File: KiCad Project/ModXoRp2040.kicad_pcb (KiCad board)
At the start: 2 copper layers, 38 x 34.8 mm, 0 parts

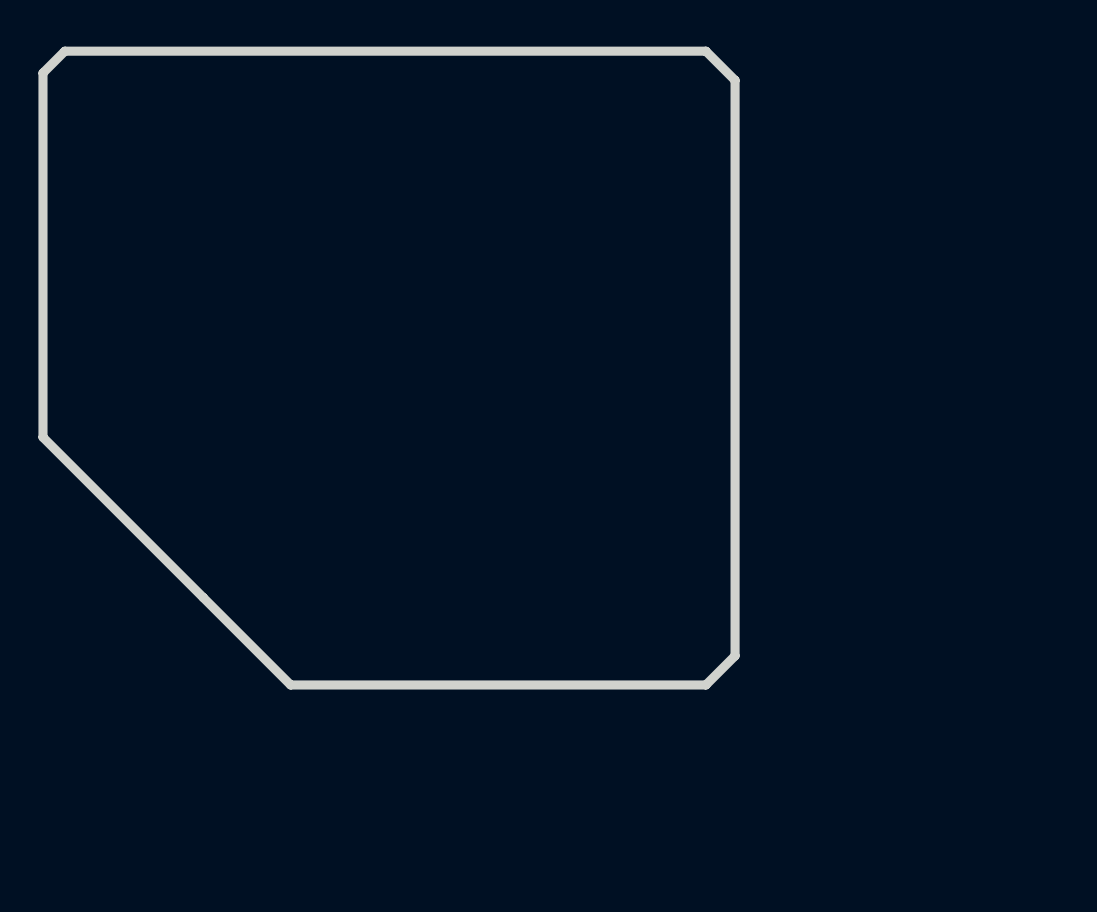
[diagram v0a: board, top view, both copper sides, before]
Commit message: finish schematics, start on pcb layout
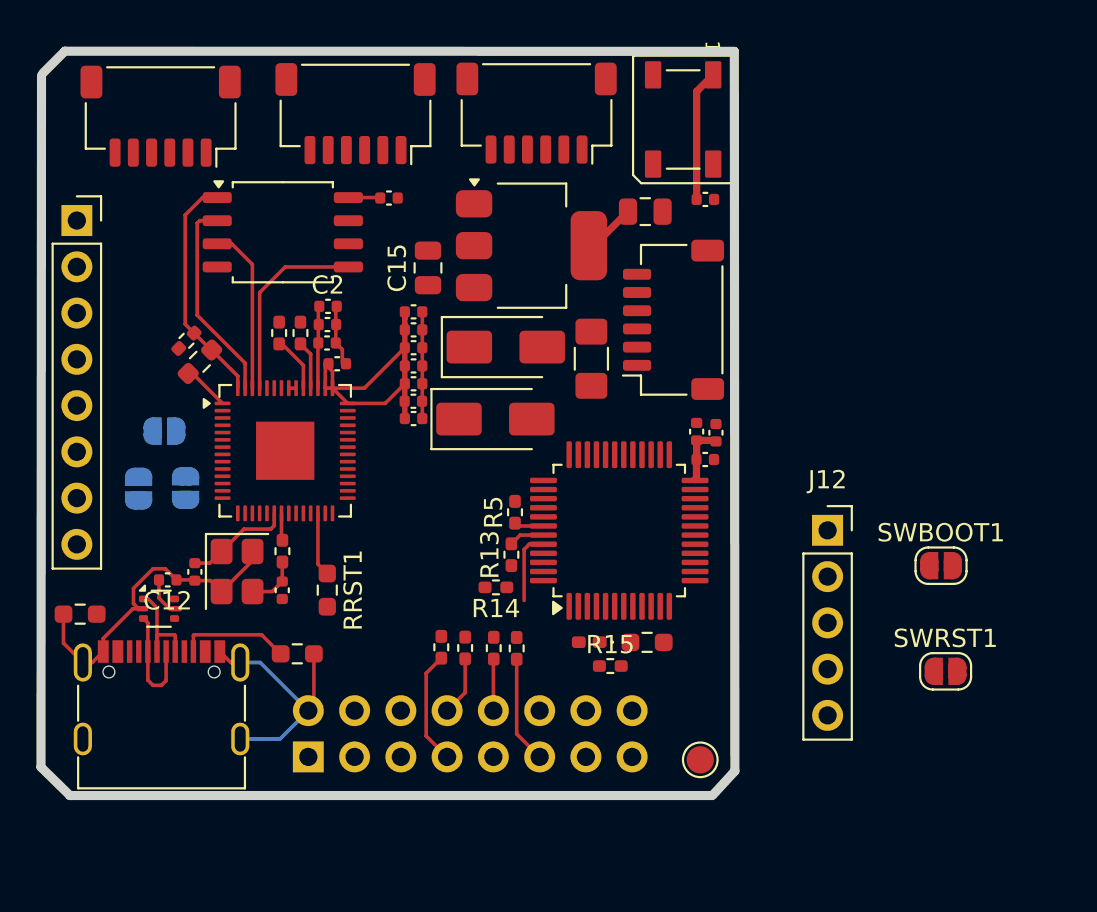
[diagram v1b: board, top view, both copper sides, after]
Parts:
- added C1: 100nF, Capacitor_SMD:C_0402_1005Metric, F.Cu at (28.0, 27.4)
- added C10: 100nF, Capacitor_SMD:C_0402_1005Metric, F.Cu at (32.7, 30.7)
- added C11: 100nF, Capacitor_SMD:C_0402_1005Metric, F.Cu at (32.7, 31.6)
- added C12: 100nF, Capacitor_SMD:C_0402_1005Metric, F.Cu at (19.2, 41.4)
- added C13: 100nF, Capacitor_SMD:C_0402_1005Metric, F.Cu at (32.7, 32.6)
- added C14: 100nF, Capacitor_SMD:C_0402_1005Metric, F.Cu at (31.4, 20.5)
- added C15: 10uF, Capacitor_SMD:C_0805_2012Metric, F.Cu at (33.5, 24.3)
- added C16: 10uF, Capacitor_SMD:C_0805_2012Metric, F.Cu at (45.5, 21.2)
- added C17: 100nF, Capacitor_SMD:C_0402_1005Metric, F.Cu at (48.3, 33.3)
- added C18: 100nF, Capacitor_SMD:C_0402_1005Metric, F.Cu at (49.4, 33.4)
- added C19: 1uF, Capacitor_SMD:C_0402_1005Metric, F.Cu at (48.8, 34.8)
- added C2: 100nF, Capacitor_SMD:C_0402_1005Metric, F.Cu at (28.1, 26.4)
- added C20: 100nF, Capacitor_SMD:C_0402_1005Metric, F.Cu at (48.8, 20.5)
- added C3: 1uF, Capacitor_SMD:C_0402_1005Metric, F.Cu at (28.0, 28.4)
- added C5: 1uF, Capacitor_SMD:C_0402_1005Metric, F.Cu at (28.6, 29.6)
- added C6: 100nF, Capacitor_SMD:C_0402_1005Metric, F.Cu at (32.7, 26.7)
- added C7: 100nF, Capacitor_SMD:C_0402_1005Metric, F.Cu at (32.7, 27.7)
- added C8: 100nF, Capacitor_SMD:C_0402_1005Metric, F.Cu at (32.7, 28.7)
- added C9: 100nF, Capacitor_SMD:C_0402_1005Metric, F.Cu at (32.7, 29.7)
- added CXTAL1: 30pF, Capacitor_SMD:C_0402_1005Metric, F.Cu at (20.7, 41.0)
- added CXTAL2: 30pF, Capacitor_SMD:C_0402_1005Metric, F.Cu at (25.5, 42.0)
- added D1: D_Schottky, Diode_SMD:D_SMA, F.Cu at (37.2, 32.6)
- added D3: WS2812B, LED_SMD:LED_WS2812B_PLCC4_5.0x5.0mm_P3.2mm, F.Cu at (47.5, 16.1)
- added D4: STM_LED2, LED_SMD:LED_0402_1005Metric_Pad0.77x0.64mm_HandSolder, F.Cu at (42.4, 44.9)
- added D5: SS34, Diode_SMD:D_SMA, F.Cu at (37.8, 28.6)
- added FU1: 0.5A, Fuse:Fuse_1206_3216Metric_Pad1.42x1.75mm_HandSolder, F.Cu at (42.5, 29.3)
- added J1: LPC, Connector_PinSocket_2.54mm:PinSocket_2x08_P2.54mm_Vertical, B.Cu at (27.0, 51.1)
- added J10: STM EN SCL, Jumper:SolderJumper-2_P1.3mm_Open_RoundedPad1.0x1.5mm, B.Cu at (17.6, 36.4)
- added J11: USB_C_Receptacle_USB2.0, Connector_USB:USB_C_Receptacle_G-Switch_GT-USB-7010ASV, F.Cu at (18.9, 49.1)
- added J12: Conn_01x05, Connector_PinSocket_2.54mm:PinSocket_1x05_P2.54mm_Vertical, F.Cu at (55.5, 38.7)
- added J13: Display Exp, Connector_JST:JST_SH_SM06B-SRSS-TB_1x06-1MP_P1.00mm_Horizontal, F.Cu at (18.9, 16.0)
- added J2: PROG SM32, Connector_PinSocket_2.54mm:PinSocket_1x08_P2.54mm_Vertical, F.Cu at (14.3, 21.7)
- added J3: STM EN, Jumper:SolderJumper-2_P1.3mm_Open_RoundedPad1.0x1.5mm, B.Cu at (20.2, 36.4)
- added J4: RGB Exp, Connector_JST:JST_SH_SM06B-SRSS-TB_1x06-1MP_P1.00mm_Horizontal, F.Cu at (29.6, 15.8)
- added J5: I2C Exp, Connector_JST:JST_SH_SM06B-SRSS-TB_1x06-1MP_P1.00mm_Horizontal, F.Cu at (39.5, 15.8)
- added J6: STM Dbg, Connector_JST:JST_SH_SM06B-SRSS-TB_1x06-1MP_P1.00mm_Horizontal, F.Cu at (47.0, 27.1)
- added J8: D0, TestPoint:TestPoint_Pad_D1.5mm, F.Cu at (48.5, 51.3)
- added J9: STM EN SDA, Jumper:SolderJumper-2_P1.3mm_Open_RoundedPad1.0x1.5mm, B.Cu at (19.1, 33.3)
- added R1: 100, Resistor_SMD:R_0402_1005Metric_Pad0.72x0.64mm_HandSolder, F.Cu at (34.3, 45.1)
- added R10: 10K, Resistor_SMD:R_0603_1608Metric_Pad0.98x0.95mm_HandSolder, F.Cu at (21.0, 29.5)
- added R11: 1K, Resistor_SMD:R_0402_1005Metric_Pad0.72x0.64mm_HandSolder, F.Cu at (25.5, 39.9)
- added R12: 5.1k, Resistor_SMD:R_0603_1608Metric_Pad0.98x0.95mm_HandSolder, F.Cu at (26.4, 45.5)
- added R13: 2k, Resistor_SMD:R_0402_1005Metric_Pad0.72x0.64mm_HandSolder, F.Cu at (38.1, 40.0)
- added R14: 2k, Resistor_SMD:R_0402_1005Metric_Pad0.72x0.64mm_HandSolder, F.Cu at (37.3, 41.8)
- added R15: 2k, Resistor_SMD:R_0402_1005Metric_Pad0.72x0.64mm_HandSolder, F.Cu at (43.5, 46.2)
- added R16: 1K, Resistor_SMD:R_0603_1608Metric_Pad0.98x0.95mm_HandSolder, F.Cu at (45.6, 44.9)
- added R2: 100, Resistor_SMD:R_0402_1005Metric_Pad0.72x0.64mm_HandSolder, F.Cu at (38.4, 45.2)
- added R3: 100, Resistor_SMD:R_0402_1005Metric_Pad0.72x0.64mm_HandSolder, F.Cu at (37.1, 45.2)
- added R4: 100, Resistor_SMD:R_0402_1005Metric_Pad0.72x0.64mm_HandSolder, F.Cu at (35.6, 45.2)
- added R5: 2k, Resistor_SMD:R_0402_1005Metric_Pad0.72x0.64mm_HandSolder, F.Cu at (38.3, 37.7)
- added R6: 5.1k, Resistor_SMD:R_0603_1608Metric_Pad0.98x0.95mm_HandSolder, F.Cu at (14.4, 43.3)
- added R7: 27, Resistor_SMD:R_0402_1005Metric_Pad0.72x0.64mm_HandSolder, F.Cu at (25.4, 27.9)
- added R8: 27, Resistor_SMD:R_0402_1005Metric_Pad0.72x0.64mm_HandSolder, F.Cu at (26.5, 27.9)
- added R9: 1K, Resistor_SMD:R_0402_1005Metric_Pad0.72x0.64mm_HandSolder, F.Cu at (20.3, 28.3)
- added RRST1: 10K, Resistor_SMD:R_0603_1608Metric_Pad0.98x0.95mm_HandSolder, F.Cu at (28.0, 42.0)
- added SWBOOT1: K2-1187SQ-C4SW-06, Jumper:SolderJumper-2_P1.3mm_Open_RoundedPad1.0x1.5mm, F.Cu at (61.7, 40.6)
- added SWRST1: K2-1187SQ-C4SW-06, Jumper:SolderJumper-2_P1.3mm_Open_RoundedPad1.0x1.5mm, F.Cu at (62.0, 46.5)
- added U1: RP2040, Package_DFN_QFN:QFN-56-1EP_7x7mm_P0.4mm_EP3.2x3.2mm, F.Cu at (25.7, 34.3)
- added U2: USBLC6-2P6, Package_TO_SOT_SMD:SOT-666, F.Cu at (18.8, 43.0)
- added U3: STM32F030C8Tx, Package_QFP:LQFP-48_7x7mm_P0.5mm, F.Cu at (44.0, 38.7)
- added UF1: W25Q128JVS, libs:SOIC-8_5.275x5.275mm_P1.27mm, F.Cu at (25.6, 22.3)
- added UV1: NCP1117-3.3_SOT223, Package_TO_SOT_SMD:SOT-223-3_TabPin2, F.Cu at (39.2, 23.1)
- added Y1: 12MHz, Crystal:Crystal_SMD_3225-4Pin_3.2x2.5mm, F.Cu at (23.1, 41.0)
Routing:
- net GND: track 0.00 -> 41.1 mm
- net +3V3: track 0.00 -> 27.7 mm
- net /QSPI_SS: track 0.00 -> 12.9 mm
- net /QSPI_SD1: track 0.00 -> 11.3 mm
- net /QSPI_SD0: track 0.00 -> 10.7 mm
- net /QSPI_SD2: track 0.00 -> 9.19 mm
- net +5V: track 0.00 -> 7.22 mm
- net Net-(J11-D--PadA7): track 0.00 -> 6.31 mm
- net Net-(J1-Pin_7): track 0.00 -> 6.24 mm
- net Net-(J11-D+-PadA6): track 0.00 -> 6.20 mm
- net Net-(J11-CC2): track 0.00 -> 6.12 mm
- net /XIN: track 0.00 -> 5.89 mm
- net Net-(J1-Pin_11): track 0.00 -> 5.88 mm
- net +1V1: track 0.00 -> 4.52 mm
- net Net-(U3-BOOT0): track 0.00 -> 3.98 mm
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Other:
- board size 38 x 34.8 mm -> 38.1 x 40.9 mm

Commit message: continue layout, put some tracks down
need to rotate rp2040 otherwise layout is pretty much final?
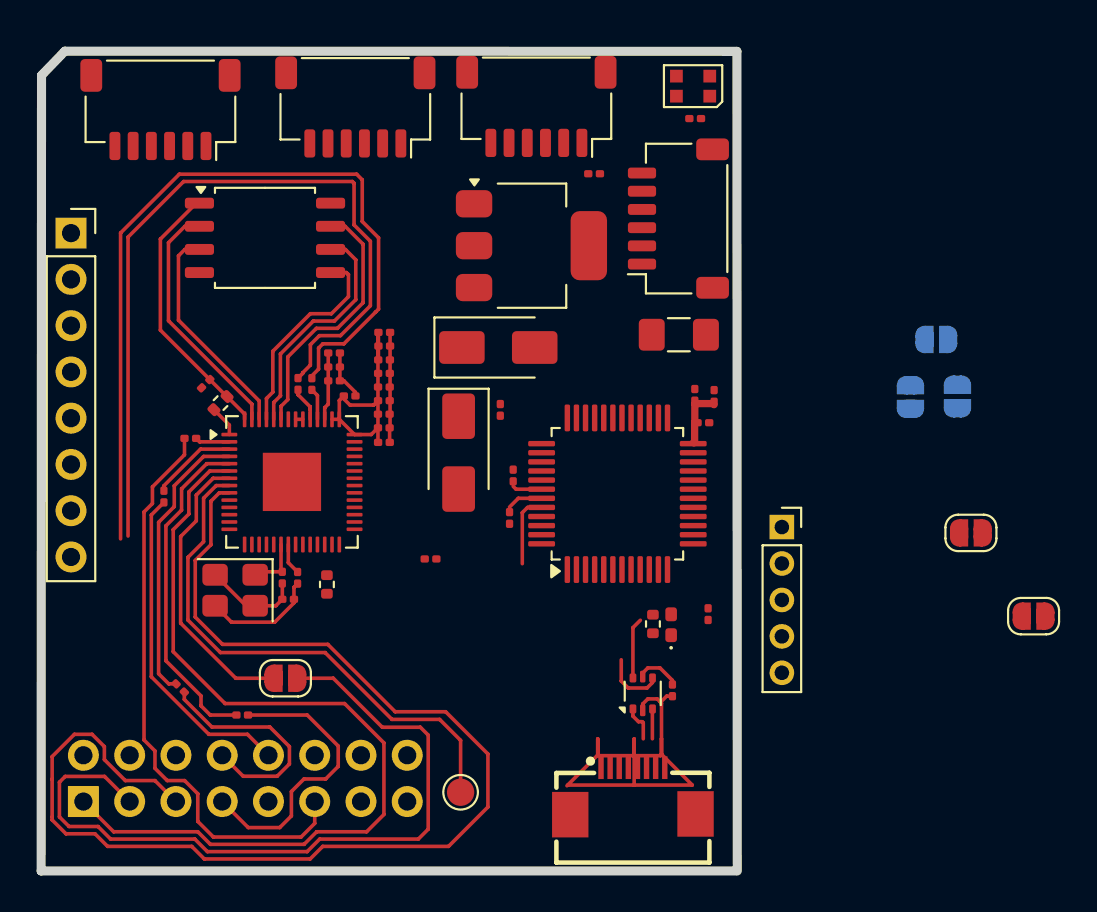
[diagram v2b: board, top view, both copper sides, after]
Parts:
- removed D3: WS2812B, LED_SMD:LED_WS2812B_PLCC4_5.0x5.0mm_P3.2mm
- removed J11: USB_C_Receptacle_USB2.0, Connector_USB:USB_C_Receptacle_G-Switch_GT-USB-7010ASV
- removed R12, R6: 5.1k, Resistor_SMD:R_0603_1608Metric_Pad0.98x0.95mm_HandSolder
- added C4: 100nF, Capacitor_SMD:C_0201_0603Metric, F.Cu at (31.1, 27.8)
- added D2: WS2812B-2020, LED_SMD:LED_WS2812B-2020_PLCC4_2.0x2.0mm, F.Cu at (48.1, 14.3)
- added FPC1: FPC-05F-8PH20, fpc:FPC-SMD_8P-P0.50_FPC-05F-8PH20, F.Cu at (44.8, 53.0)
- added J7: 1.6 EN, Jumper:SolderJumper-2_P1.3mm_Open_RoundedPad1.0x1.5mm, F.Cu at (25.7, 46.8)
- C1, C10, C11, C12, C13, C14, C17, C18, C19, C2, C20, C3, C5, C6, C7, C8, C9, CXTAL1, CXTAL2: footprint Capacitor_SMD:C_0402_1005Metric -> Capacitor_SMD:C_0201_0603Metric
- C15, C16: footprint Capacitor_SMD:C_0805_2012Metric -> Capacitor_SMD:C_0201_0603Metric
- J12: footprint Connector_PinSocket_2.54mm:PinSocket_1x05_P2.54mm_Vertical -> Connector_PinSocket_2.00mm:PinSocket_1x05_P2.00mm_Vertical
- R1, R11, R13, R14, R15, R2, R3, R4, R5, R7, R8, R9: footprint Resistor_SMD:R_0402_1005Metric_Pad0.72x0.64mm_HandSolder -> Resistor_SMD:R_0201_0603Metric
- R10, R16, RRST1: footprint Resistor_SMD:R_0603_1608Metric_Pad0.98x0.95mm_HandSolder -> Resistor_SMD:R_0402_1005Metric
- UF1: footprint libs:SOIC-8_5.275x5.275mm_P1.27mm -> fpc:SOIC-8_5.275x5.275mm_P1.27mm
- moved J10 42.7 mm to (60.0, 31.4)
- moved J9 42.7 mm to (61.5, 28.2)
- moved J3 42.7 mm to (62.6, 31.4)
- moved C12 28.4 mm to (47.0, 47.5), turned to 90 degrees
- moved U2 27.0 mm to (45.3, 47.7), turned to 90 degrees
- moved R2 21.3 mm to (20.5, 33.7), turned to 180 degrees
- moved R3 19.9 mm to (19.0, 36.9)
- moved R4 15.8 mm to (19.9, 47.4), turned to -45 degrees
- moved C14 13.4 mm to (31.1, 33.9)
- moved J8 13.3 mm to (35.3, 53.1)
- moved J1 12.6 mm to (14.6, 53.6)
- moved R1 11.5 mm to (23.3, 48.9), turned to 0 degrees
- moved C15 8.75 mm to (37.5, 32.1)
- moved R15 6.08 mm to (48.9, 43.3), turned to 90 degrees
- moved SWRST1 5.70 mm to (66.8, 43.4)
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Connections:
- J1 pad 3: /LFRAME -> /LRAME_1.6
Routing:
- net /RST: track 0.00 -> 68.7 mm
- net /USB_D-: track 0.00 -> 48.4 mm
- net /LCLK: track 0.00 -> 47.6 mm
- net /USB_D+: track 0.00 -> 46.9 mm
- net /LRAME_1.6: track 0.00 -> 41.7 mm
- net /D0: track 0.00 -> 29.3 mm
- net Net-(J1-Pin_11): track 5.88 -> 32.0 mm
- net /LAD3: track 0.00 -> 18.4 mm
- net /LFRAME: track 0.00 -> 15.9 mm
- net /LAD2: track 0.00 -> 15.6 mm
- net Net-(J1-Pin_10): track 2.84 -> 18.1 mm
- net /QSPI_SD3: track 0.00 -> 14.3 mm
- net /QSPI_SCLK: track 0.00 -> 12.9 mm
- net +3V3: track 27.7 -> 16.3 mm
- net Net-(J1-Pin_7): track 6.24 -> 15.9 mm
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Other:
- board size 38.1 x 40.9 mm -> 38.2 x 45 mm

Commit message: semi update
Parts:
- removed J7: 1.6 EN, Jumper:SolderJumper-2_P1.3mm_Open_RoundedPad1.0x1.5mm
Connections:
- J1 pad 3: /LRAME_1.6 -> /LFRAME
- J13 pad 6: unconnected-(J13-Pin_6-Pad6) -> GND
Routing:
- net /LRAME_1.6: track 41.7 -> 0.00 mm
- net /LFRAME: track 15.9 -> 57.6 mm
